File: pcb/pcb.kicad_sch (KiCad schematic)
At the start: 19 parts, among them J0 RPi, J1 AVR-ISP-6, J2 L_motors, J3 R_motors, J4 Sensor_0, J5 Sensor_1, M0 Motor_DC, M1 Motor_DC, M2 Motor_DC, M3 Motor_DC, U0 ATmega328-P, U1 DRV8800PWP, U2 DRV8800PWP

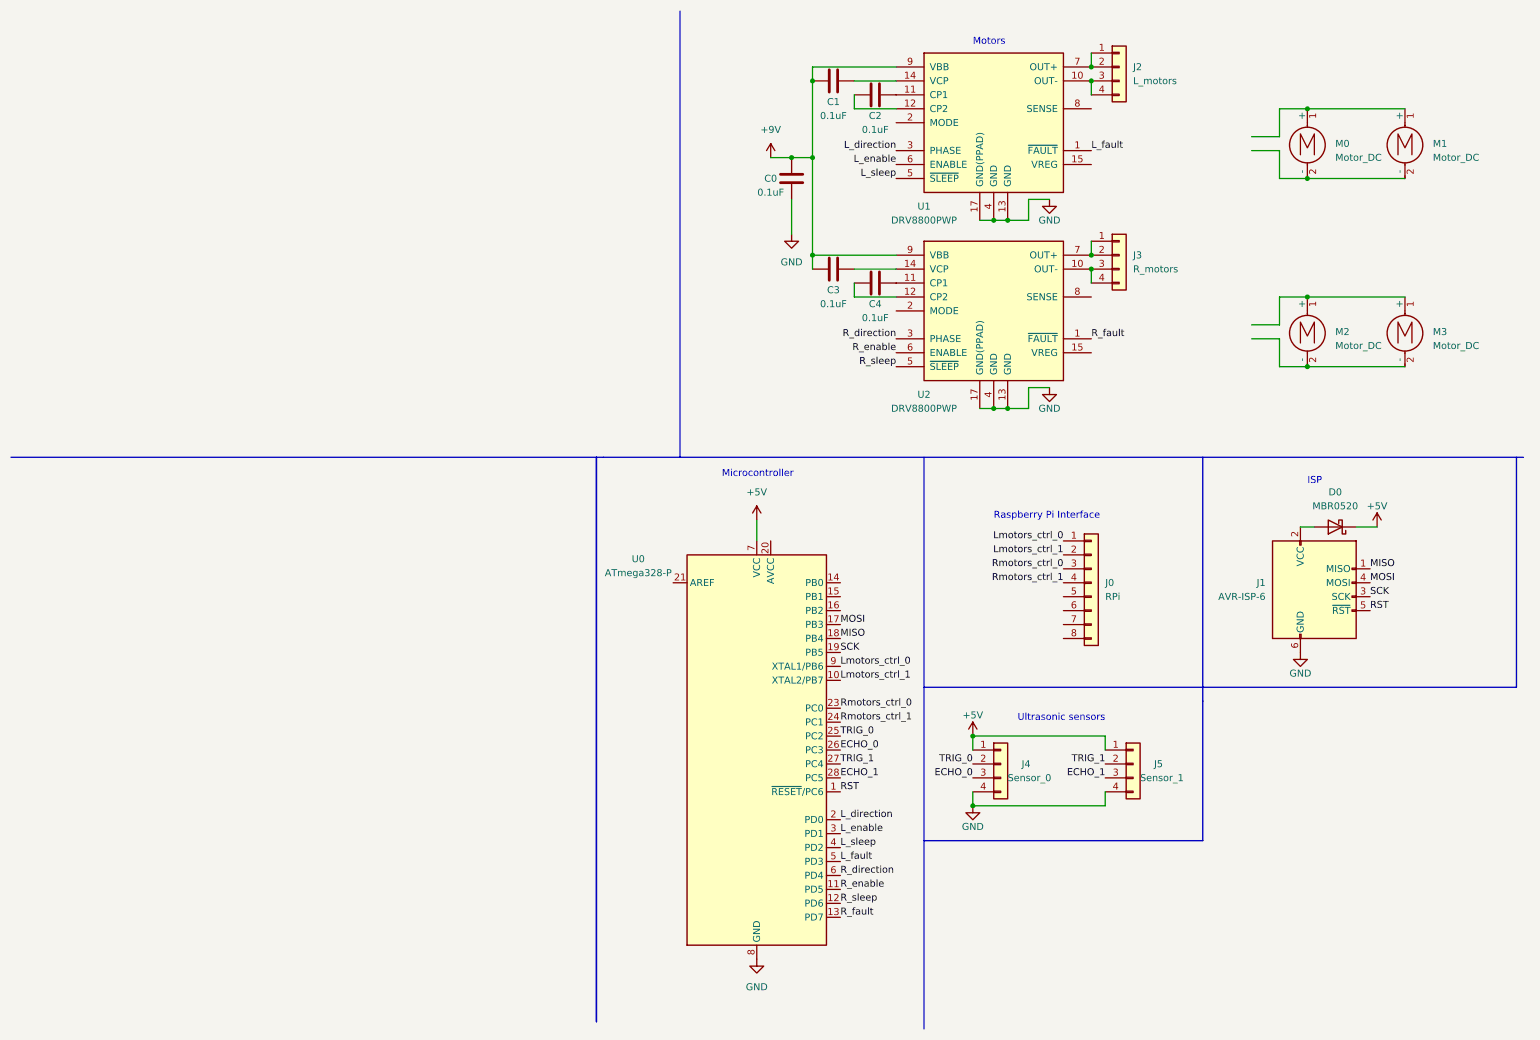
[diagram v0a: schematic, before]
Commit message: Added some skeleton files for the fetching subsystem. Updated the PCB design.
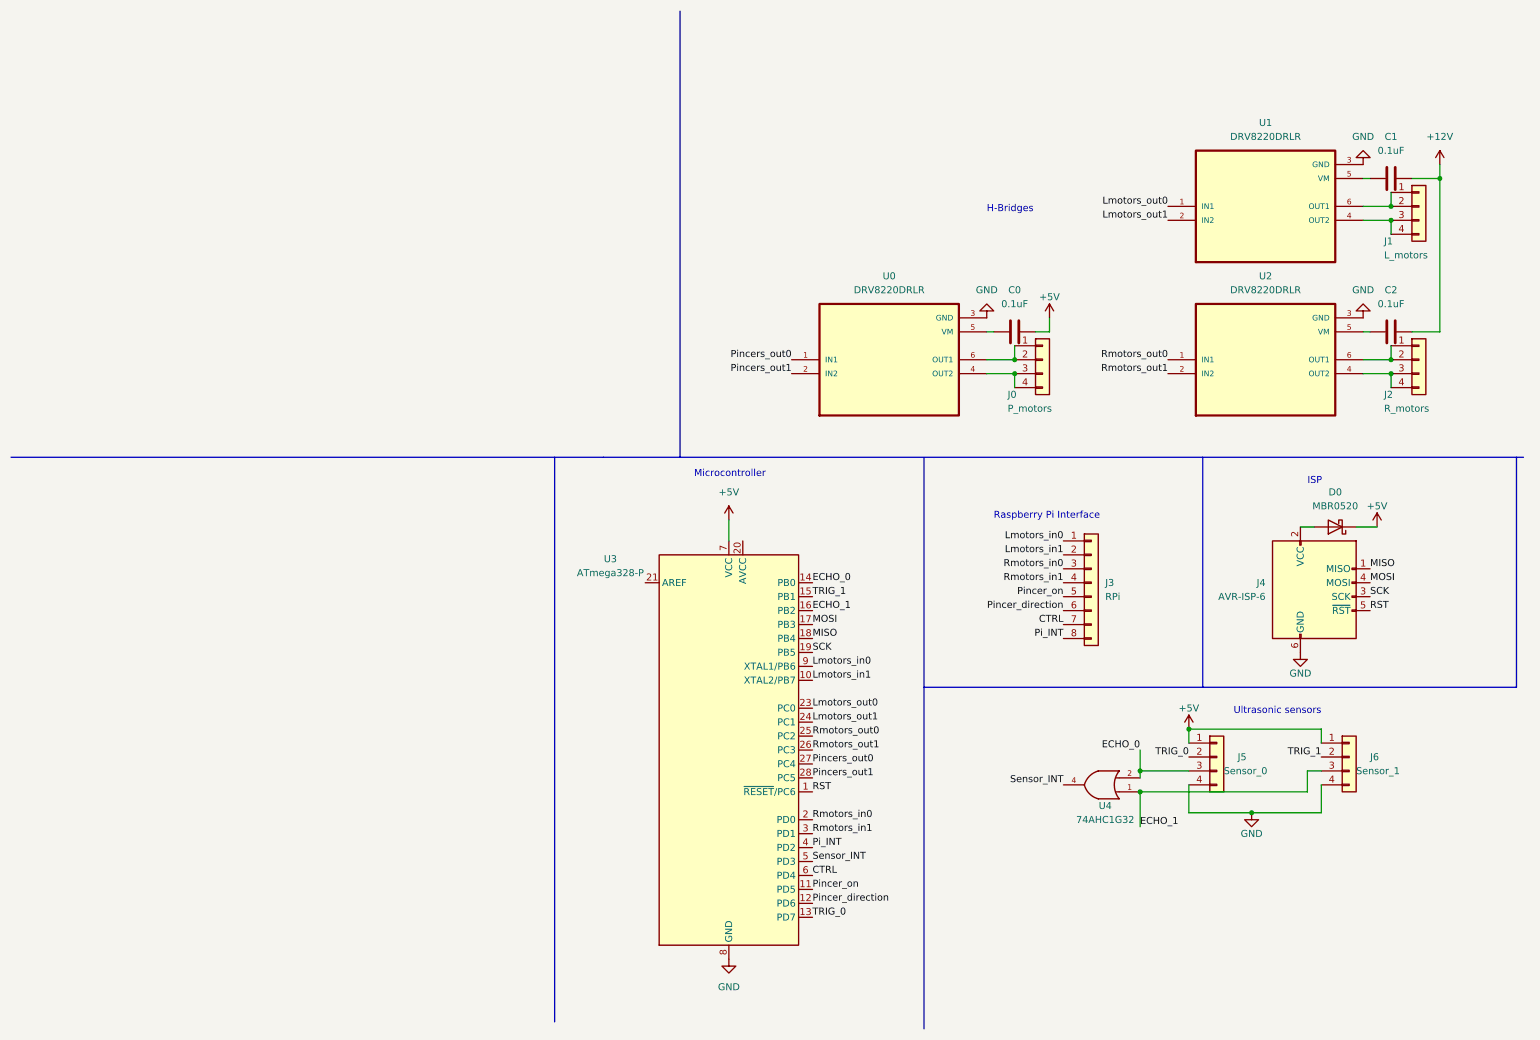
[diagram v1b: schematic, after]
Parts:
- removed C3, C4: 0.1uF, symbol Device:C
- removed M0, M1, M2, M3: Motor_DC, symbol Motor:Motor_DC
- removed U1, U2: DRV8800PWP, Package_SO:HTSSOP-16-1EP_4.4x5mm_P0.65mm_EP3.4x5mm_Mask3x3mm_ThermalVias, symbol Driver_Motor:DRV8800PWP
- added J0: P_motors, symbol Connector_Generic:Conn_01x04
- added U0, U1, U2: DRV8220DRLR, SOT50P160X60-6N, symbol DRV8220DRLR:DRV8220DRLR
- added U4: 74AHC1G32, symbol 74xGxx:74AHC1G32
- renumbered J2 to J1, J3 to J2, J0 to J3, J1 to J4, J4 to J5, J5 to J6, U0 to U3
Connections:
- net L_sleep is gone; now on net Pi_INT: U3.4 (PD2)
- net R_direction is gone; now on net CTRL: U3.6 (PD4)
- net R_enable is gone; now on net Pincer_on: U3.11 (PD5)
- net R_fault is gone; now on net TRIG_0: U3.13 (PD7)
- net R_sleep is gone; now on net Pincer_direction: U3.12 (PD6)
- net +5V: now also C0.2
- net ECHO_0: now also U3.14 (PB0), U4.2; no longer U3.26 (PC3)
- net ECHO_1: now also U3.16 (PB2), U4.1; no longer U3.28 (PC5)
- net GND: now also U0.3 (GND), U1.3 (GND), U2.3 (GND), U4.3 (GND); no longer C0.2
- net TRIG_0: no longer U3.25 (PC2)
- net TRIG_1: now also U3.15 (PB1); no longer U3.27 (PC4)
- net at J2.1 (Pin_1), J2.2 (Pin_2): now also U2.6 (OUT1)
- net at J2.3 (Pin_3), J2.4 (Pin_4): now also U2.4 (OUT2)
- net Pincer_on: now reaches J3.5 (Pin_5)
- net Pincer_direction: now reaches J3.6 (Pin_6)
- net CTRL: now reaches J3.7 (Pin_7)
- net Pi_INT: now reaches J3.8 (Pin_8)
- net at C2.1: now also U2.5 (VM)
- net +12V: now reaches C2.2
- net +12V: now also C1.2
- net at J1.3 (Pin_3), J1.4 (Pin_4): now also U1.4 (OUT2)
- net at J1.1 (Pin_1), J1.2 (Pin_2): now also U1.6 (OUT1)
- net +9V: no longer names the net of C0.1
- net +9V: now also U0.5 (VM); no longer C1.1
- net L_direction renamed Rmotors_in0
- net Rmotors_in0: now also J3.3 (Pin_3)
- net L_enable renamed Rmotors_in1
- net Rmotors_in1: now also J3.4 (Pin_4)
- net L_fault renamed Sensor_INT
- net Sensor_INT: now also U4.4
- net Lmotors_ctrl_0 renamed Lmotors_in0
- net Lmotors_ctrl_1 renamed Lmotors_in1
- net Rmotors_ctrl_0 renamed Lmotors_out0
- net Lmotors_out0: now also U1.1 (IN1); no longer J3.3 (Pin_3)
- net Rmotors_ctrl_1 renamed Lmotors_out1
- net Lmotors_out1: now also U1.2 (IN2); no longer J3.4 (Pin_4)
- new net: J0.3 (Pin_3), J0.4 (Pin_4), U0.4 (OUT2)
- new net: J0.1 (Pin_1), J0.2 (Pin_2), U0.6 (OUT1)
- new net: C1.1, U1.5 (VM)
- new net Pincers_out0: U0.1 (IN1), U3.27 (PC4)
- new net Pincers_out1: U0.2 (IN2), U3.28 (PC5)
- new net Rmotors_out0: U2.1 (IN1), U3.25 (PC2)
- new net Rmotors_out1: U2.2 (IN2), U3.26 (PC3)
- new net VCC: U4.5 (VCC)
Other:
- note added: "H-Bridges"
- note removed: "Motors"
- moved on the sheet: J1, J2, J5, J6, U3

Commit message: Added All PCB stuff
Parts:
- removed C0, C1, C2: 0.1uF, symbol Device:C
- removed U0, U1, U2: DRV8220DRLR, SOT50P160X60-6N, symbol DRV8220DRLR:DRV8220DRLR
- added C1, C4, C7: 2.2uF, Capacitor_SMD:C_1206_3216Metric_Pad1.33x1.80mm_HandSolder, symbol Device:C_Small
- added C2, C5, C8: 10uF, Capacitor_SMD:C_1210_3225Metric_Pad1.33x2.70mm_HandSolder, symbol Device:C_Small
- added C3, C6, C9: 0.1uF, Capacitor_SMD:C_1812_4532Metric_Pad1.57x3.40mm_HandSolder, symbol Device:C_Small
- added H1, H2, H3, H4: MountingHole, MountingHole:MountingHole_3.2mm_M3, symbol Mechanical:MountingHole
- added J7: Vin, Connector_Molex:Molex_KK-254_AE-6410-02A_1x02_P2.54mm_Vertical, symbol Connector_Generic:Conn_01x02
- added R1, R2, R3: 5k, Resistor_SMD:R_1206_3216Metric_Pad1.30x1.75mm_HandSolder, symbol Device:R
- added TP1, TP10, TP2, TP3, TP4, TP5, TP6, TP7, TP8, TP9: TestPoint, TestPoint:TestPoint_Pad_1.5x1.5mm, symbol Connector:TestPoint
- added U0, U1, U2: DRV8848, Package_SO:TSSOP-16-1EP_4.4x5mm_P0.65mm, symbol Driver_Motor:DRV8848
- added U5, U6: TDN_5-0911WISM, Converter_DCDC:Converter_DCDC_TRACO_TDN_5-xxxxWISM_SMD, symbol Regulator_Switching:TDN_5-0911WISM
- J0, J1, J2, J5, J6: footprint (none) -> Connector_PinSocket_2.54mm:PinSocket_1x04_P2.54mm_Vertical_SMD_Pin1Left
- J3: footprint (none) -> Connector_PinSocket_2.54mm:PinSocket_1x08_P2.54mm_Vertical_SMD_Pin1Left
- J4: footprint (none) -> Connector_IDC:IDC-Header_2x03_P2.54mm_Vertical
- U4: footprint (none) -> Package_TO_SOT_SMD:SOT-23-5_HandSoldering
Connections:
- net +12V: now also J7.2 (Pin_2), TP1.1, U5.1 (+VIN), U6.1 (+VIN)
- net +5V: now also C8.1, C9.1, TP2.1, TP3.1, TP6.1, U0.1 (nSLEEP), U0.12 (VM), U1.1 (nSLEEP), U2.1 (nSLEEP), U5.7 (+VOUT)
- net GND: now also C1.1, C2.2, C3.2, C4.1, C5.2, C6.2, C7.1, C8.2, C9.2, J7.1 (Pin_1), U0.13 (GND), U0.17 (PPAD), U0.3 (AISEN), U0.6 (BISEN), U1.13 (GND), U1.17 (PPAD), U1.3 (AISEN), U1.6 (BISEN), U2.13 (GND), U2.17 (PPAD), U2.3 (AISEN), U2.6 (BISEN), U5.2 (-VIN), U6.2 (-VIN)
- net Lmotors_out0: now also U1.16 (AIN1), U1.9 (BIN1)
- net Lmotors_out1: now also U1.10 (BIN2), U1.15 (AIN2)
- net Pincers_out0: now also U0.16 (AIN1), U0.9 (BIN1)
- net Pincers_out1: now also U0.10 (BIN2), U0.15 (AIN2)
- net Rmotors_out0: now also U2.16 (AIN1), U2.9 (BIN1)
- net Rmotors_out1: now also U2.10 (BIN2), U2.15 (AIN2)
- net at J0.4 (Pin_4): now also TP5.1, U0.5 (BOUT2); no longer J0.3 (Pin_3)
- net at J0.1 (Pin_1): now also TP4.1, U0.2 (AOUT1); no longer J0.2 (Pin_2)
- net at J2.1 (Pin_1): now also TP7.1, U2.2 (AOUT1); no longer J2.2 (Pin_2)
- net at J2.3 (Pin_3): now also U2.7 (BOUT1); no longer J2.4 (Pin_4)
- net at J1.4 (Pin_4): now also TP8.1, U1.5 (BOUT2); no longer J1.3 (Pin_3)
- net at J1.1 (Pin_1): now also TP10.1, U1.2 (AOUT1); no longer J1.2 (Pin_2)
- new net: J2.2 (Pin_2), U2.4 (AOUT2)
- new net: J2.4 (Pin_4), TP9.1, U2.5 (BOUT2)
- new net: J1.2 (Pin_2), U1.4 (AOUT2)
- new net: J1.3 (Pin_3), U1.7 (BOUT1)
- new net: R1.2, U1.8 (nFAULT)
- new net: J0.2 (Pin_2), U0.4 (AOUT2)
- new net: J0.3 (Pin_3), U0.7 (BOUT1)
- new net: R3.2, U0.8 (nFAULT)
- new net: R2.2, U2.8 (nFAULT)
- new net +5VA: C2.1, C3.1, C5.1, C6.1, U1.12 (VM), U2.12 (VM), U6.7 (+VOUT)
- new net VINT: C1.2, R1.1, U1.11 (VREF), U1.14 (VINT)
- new net VINT2: C4.2, R2.1, U2.11 (VREF), U2.14 (VINT)
- new net VINT3: C7.2, R3.1, U0.11 (VREF), U0.14 (VINT)
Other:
- note added: "Power"

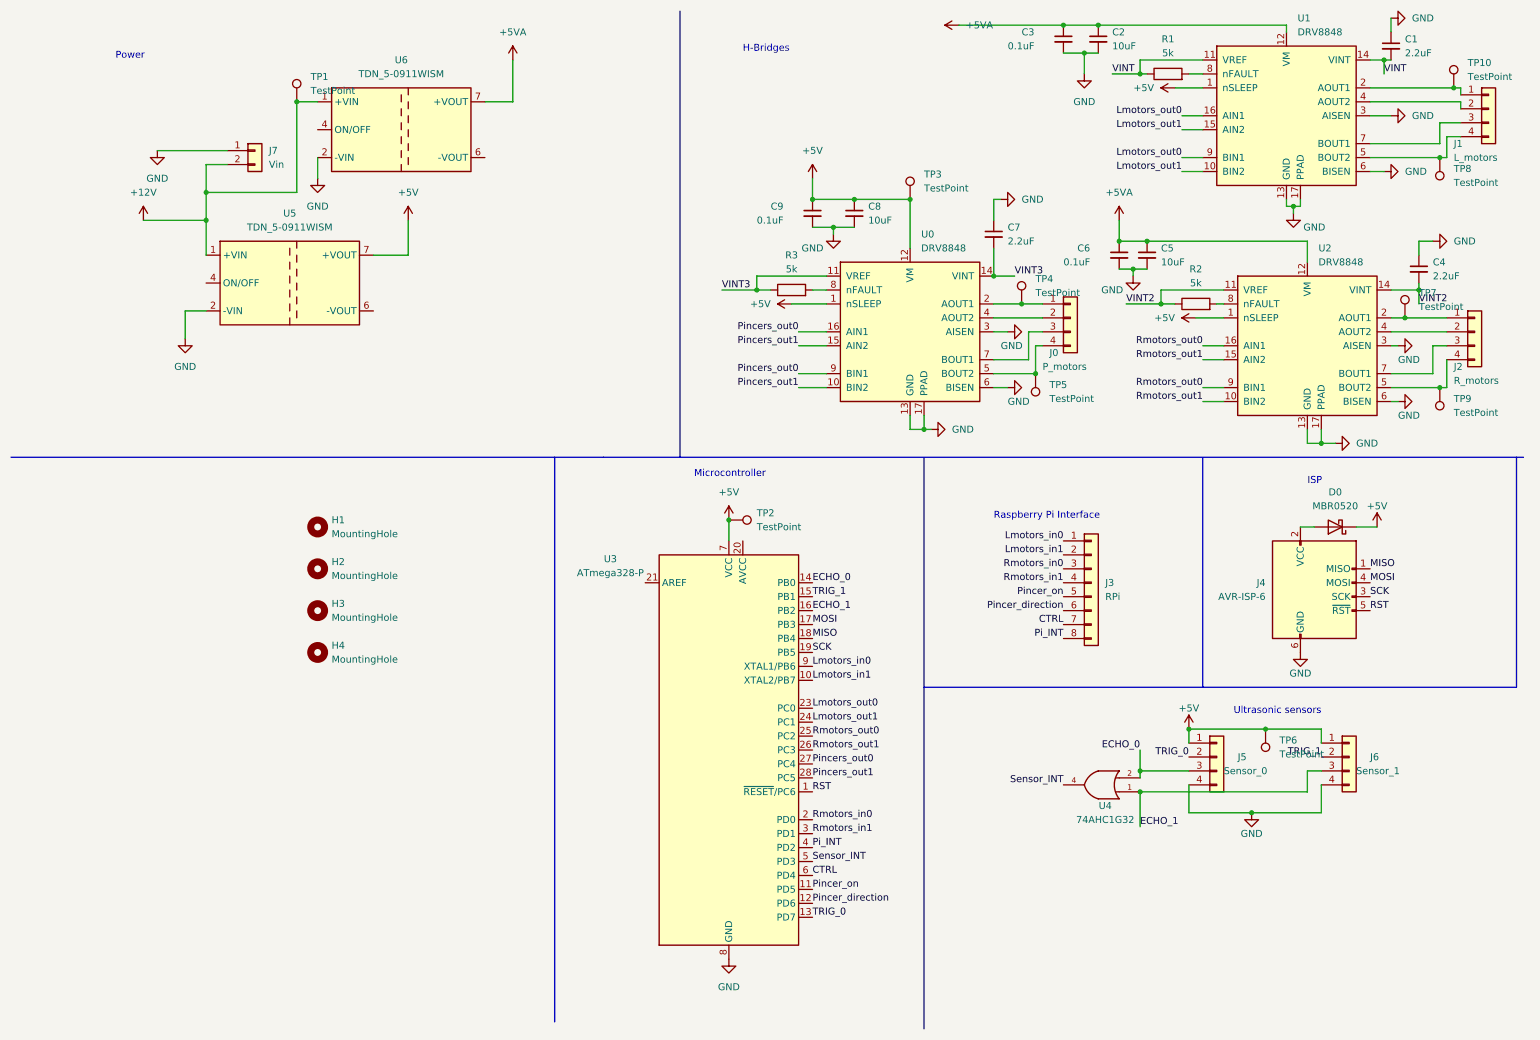
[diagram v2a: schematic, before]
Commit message: Adding the final version of the PCB blueprint
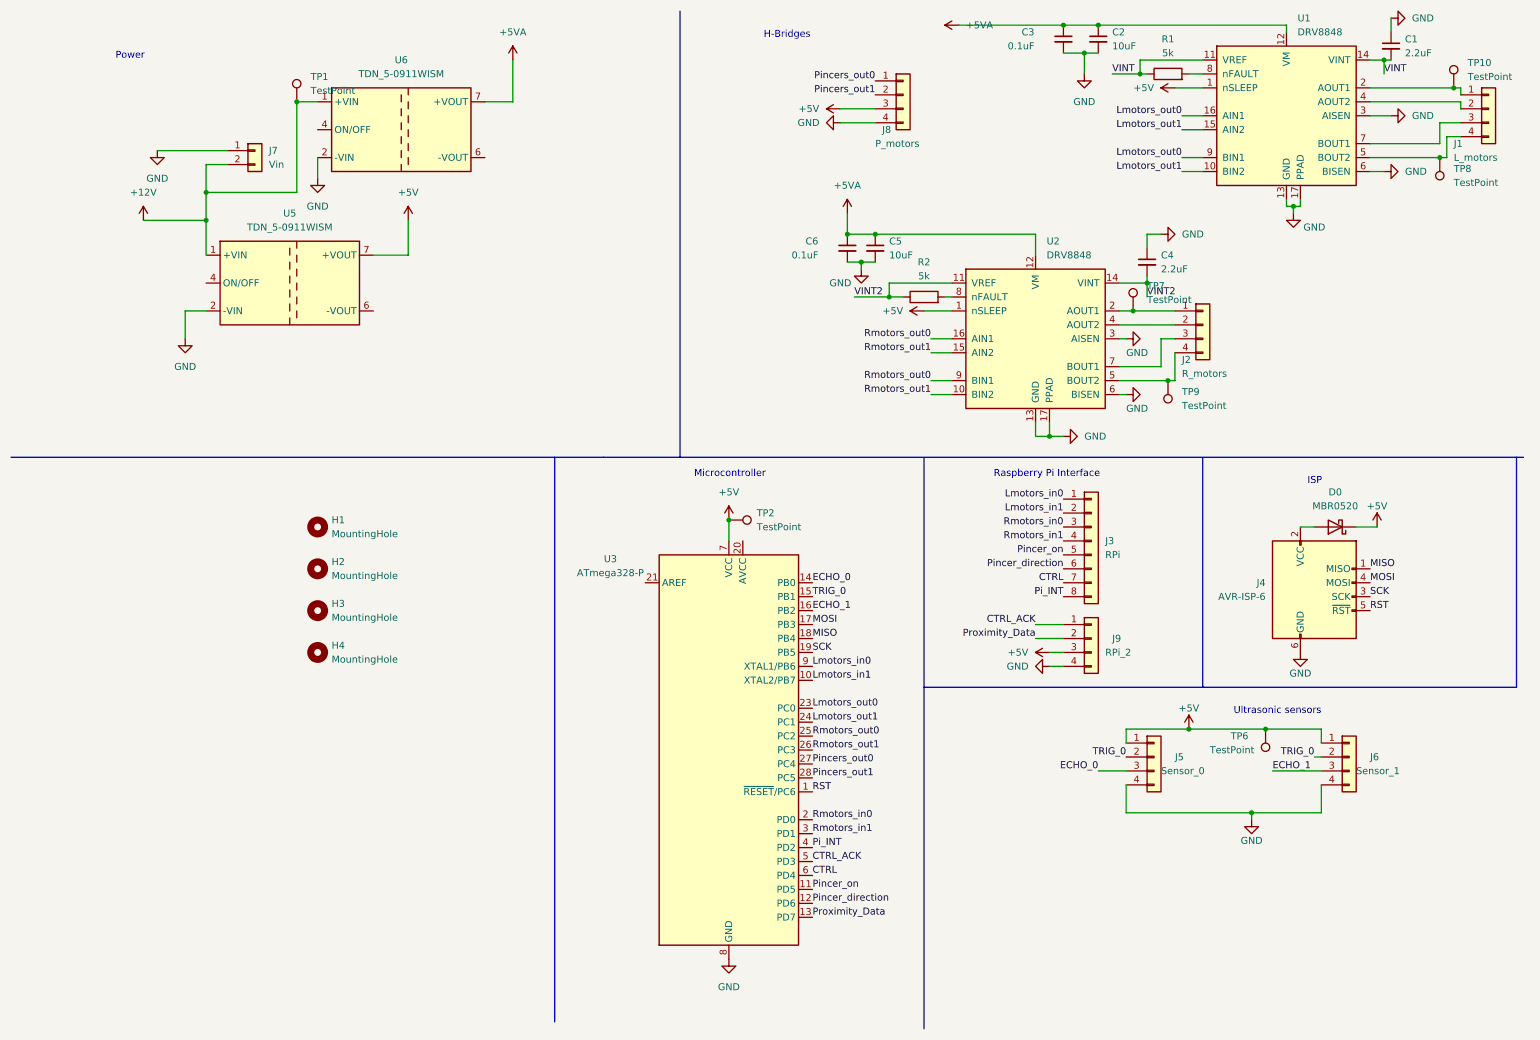
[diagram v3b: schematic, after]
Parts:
- removed C7: 2.2uF, Capacitor_SMD:C_1206_3216Metric_Pad1.33x1.80mm_HandSolder, symbol Device:C_Small
- removed C8: 10uF, Capacitor_SMD:C_1210_3225Metric_Pad1.33x2.70mm_HandSolder, symbol Device:C_Small
- removed C9: 0.1uF, Capacitor_SMD:C_1812_4532Metric_Pad1.57x3.40mm_HandSolder, symbol Device:C_Small
- removed J0: P_motors, Connector_PinSocket_2.54mm:PinSocket_1x04_P2.54mm_Vertical_SMD_Pin1Left, symbol Connector_Generic:Conn_01x04
- removed R3: 5k, Resistor_SMD:R_1206_3216Metric_Pad1.30x1.75mm_HandSolder, symbol Device:R
- removed TP3, TP4, TP5: TestPoint, TestPoint:TestPoint_Pad_1.5x1.5mm, symbol Connector:TestPoint
- removed U0: DRV8848, Package_SO:TSSOP-16-1EP_4.4x5mm_P0.65mm, symbol Driver_Motor:DRV8848
- removed U4: 74AHC1G32, Package_TO_SOT_SMD:SOT-23-5_HandSoldering, symbol 74xGxx:74AHC1G32
- added J8: P_motors, Connector_Molex:Molex_KK-254_AE-6410-04A_1x04_P2.54mm_Vertical, symbol Connector_Generic:Conn_01x04
- added J9: RPi_2, Connector_Molex:Molex_KK-254_AE-6410-04A_1x04_P2.54mm_Vertical, symbol Connector_Generic:Conn_01x04
- J1, J2, J5, J6: footprint Connector_PinSocket_2.54mm:PinSocket_1x04_P2.54mm_Vertical_SMD_Pin1Left -> Connector_Molex:Molex_KK-254_AE-6410-04A_1x04_P2.54mm_Vertical
- J3: footprint Connector_PinSocket_2.54mm:PinSocket_1x08_P2.54mm_Vertical_SMD_Pin1Left -> Connector_PinSocket_2.54mm:PinSocket_1x08_P2.54mm_Vertical_SMD_Pin1Right
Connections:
- net TRIG_1 is gone; now on net TRIG_0: J6.2 (Pin_2), U3.15 (PB1)
- net +5V: now also J8.3 (Pin_3), J9.3 (Pin_3)
- net GND: now also J8.4 (Pin_4), J9.4 (Pin_4)
- net Pincers_out0: now also J8.1 (Pin_1)
- net Pincers_out1: now also J8.2 (Pin_2)
- net TRIG_0: no longer U3.13 (PD7)
- net Sensor_INT renamed CTRL_ACK
- net CTRL_ACK: now also J9.1 (Pin_1)
- new net Proximity_Data: J9.2 (Pin_2), U3.13 (PD7)
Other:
- moved on the sheet: C4, C5, C6, J2, J3, J5, R2, TP7, TP9, U2
